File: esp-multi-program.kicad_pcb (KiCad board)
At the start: 2 copper layers, 76.2 x 50.8 mm, 11 parts, among them P1 CONN_01X08, P2 CONN_01X08, P3 CONN_01X06, P4 CONN_01X02, SW1 PTS645, SW2 PTS645, U1 ESP-12E

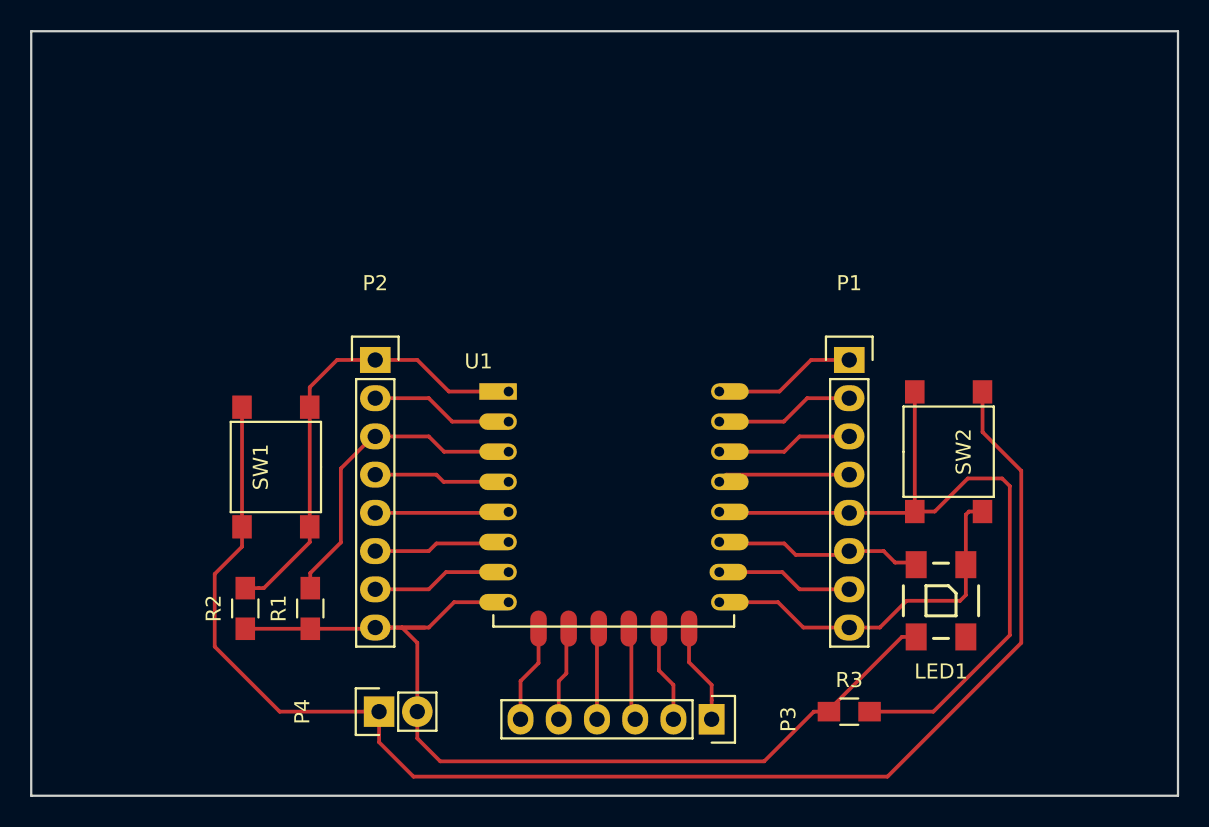
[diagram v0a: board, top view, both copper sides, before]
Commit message: Fixing resistors and adding headers
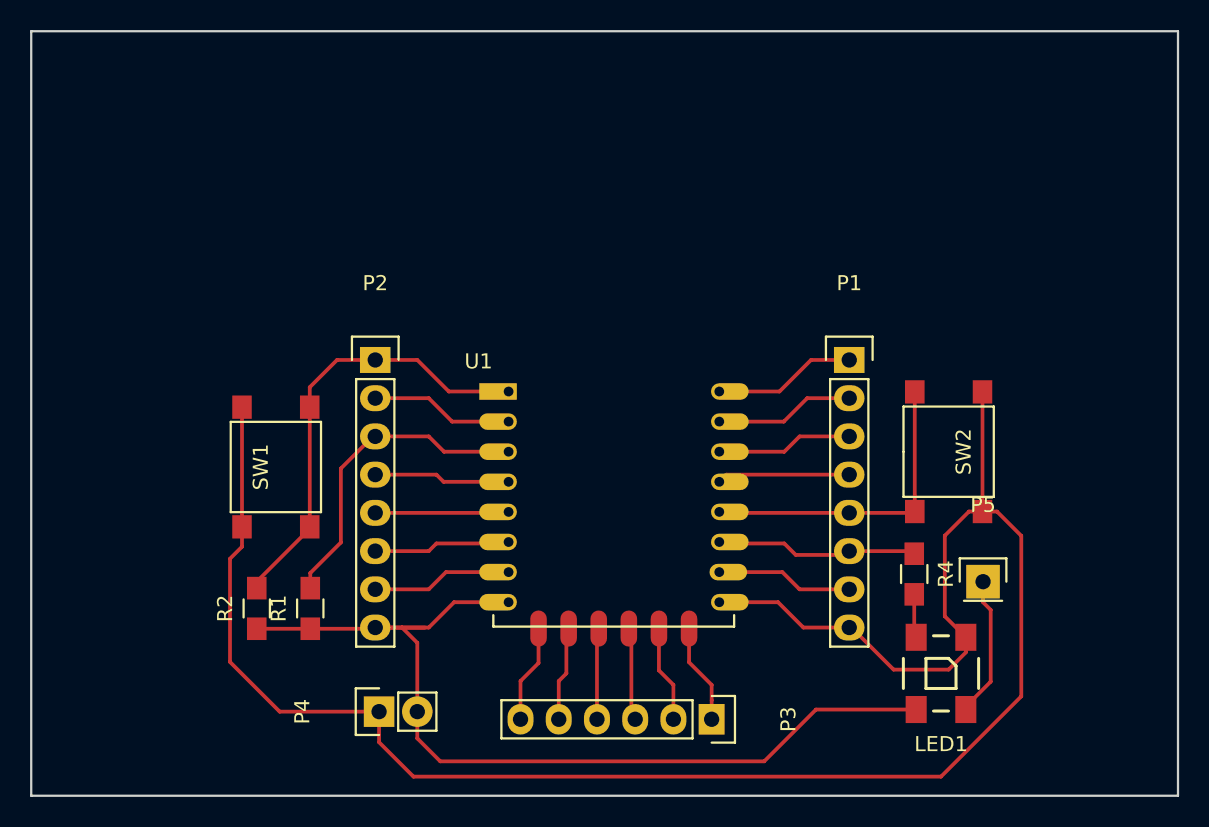
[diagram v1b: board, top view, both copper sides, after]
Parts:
- removed R3: R, Resistors_SMD:R_0805_HandSoldering
- added P5: CONN_01X01, Pin_Headers:Pin_Header_Straight_1x01, F.Cu at (164.8, 112.8)
- added R4: 220, Resistors_SMD:R_0805_HandSoldering, F.Cu at (160.3, 112.3)
- R1, R2: value R -> 2.2K
- moved LED1 4.83 mm to (162.1, 118.9)
- moved R2 0.76 mm to (116.6, 114.6)
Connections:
- LED1 pad 4: /GPIO_2 -> Net-(LED1-Pad4)
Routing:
- net /GPIO_0: track 49.9 -> 21.0 mm
- net Net-(LED1-Pad2): track 0.00 -> 9.39 mm
- net GND: track 121.0 -> 128.5 mm
- net Net-(LED1-Pad4): track 0.00 -> 2.91 mm
- net +3V3: track 66.6 -> 63.8 mm
- net /RESET: track 30.8 -> 29.9 mm
